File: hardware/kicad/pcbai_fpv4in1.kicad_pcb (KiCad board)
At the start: 6 copper layers, 85 x 70 mm, 253 parts, among them J1 BATT_PAD, J10 INA186A3IDCKR, J11 INA186A3IDCKR, J12 INA186A3IDCKR, J13 AT32F421K8T7, J14 DRV8300DRGER, J15 INA186A3IDCKR, J16 INA186A3IDCKR, J17 INA186A3IDCKR, J18 AT32F421K8T7, J19 DRV8300DRGER, J2 LMR51420YDDCR, J20 INA186A3IDCKR, J21 INA186A3IDCKR, J22 INA186A3IDCKR, J23 AT32F421K8T7, J24 DRV8300DRGER, J25 INA186A3IDCKR, J26 INA186A3IDCKR, J27 INA186A3IDCKR, J3 TLV76733DRVR, J4 SM08B-SRSS-TB, J5 USBLC6-2SC6, J6 USBLC6-2SC6, J7 USBLC6-2SC6, J8 AT32F421K8T7, J9 DRV8300DRGER, Q1 AON6260, Q10 AOTL66912, Q11 AOTL66912, Q12 AOTL66912, Q13 AOTL66912, Q14 AOTL66912, Q15 AOTL66912, Q16 AOTL66912, Q17 AOTL66912, Q18 AOTL66912, Q19 AOTL66912, Q2 AON6260, Q20 AOTL66912, Q21 AOTL66912, Q22 AOTL66912, Q23 AOTL66912, Q24 AOTL66912, Q25 AOTL66912, Q26 AOTL66912, Q27 AOTL66912, Q28 AOTL66912, Q3 AON6260, Q4 AON6260, Q5 AOTL66912, Q6 AOTL66912, Q7 AOTL66912, Q8 AOTL66912, Q9 AOTL66912

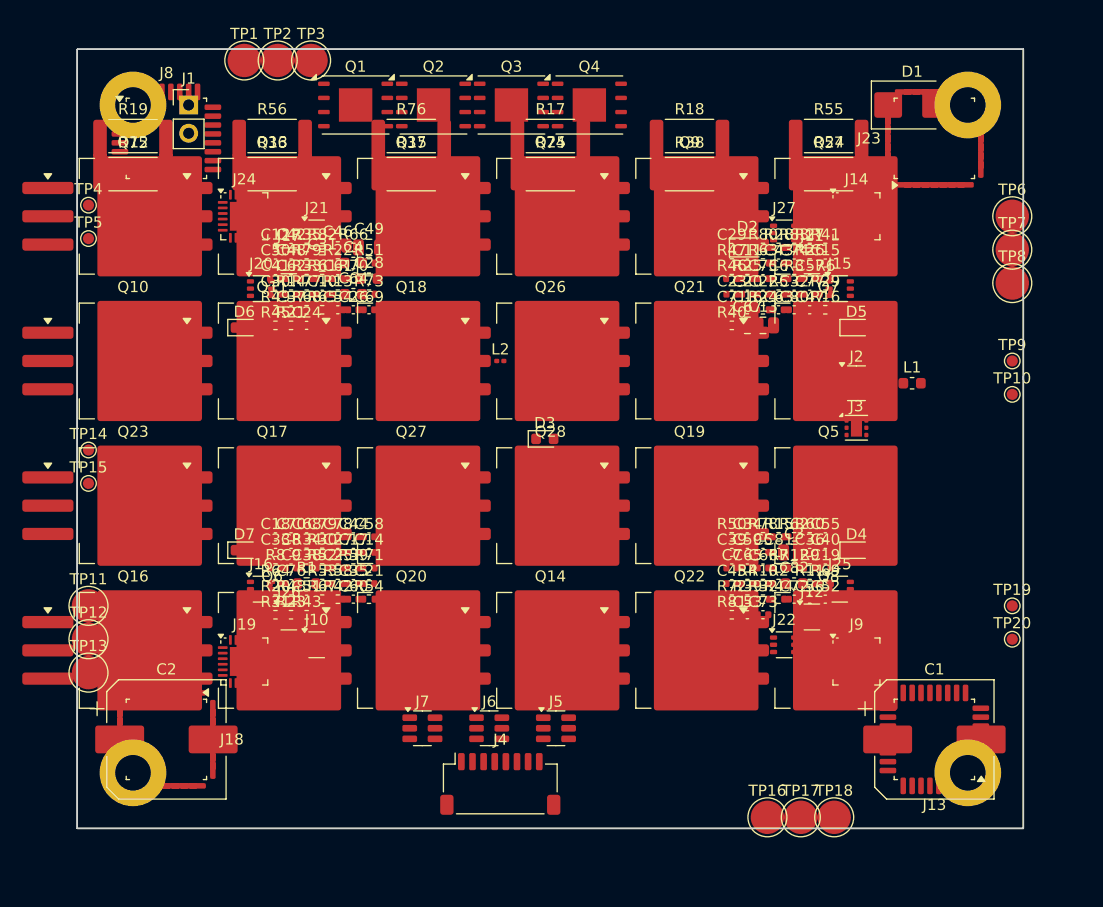
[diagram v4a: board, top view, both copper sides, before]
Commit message: Phase 4b-redo2: BEC placement integration (board 85×70 → 90×75)
Per master adjudication 2026-05-22: absorbed all Phase 2d-REDO BEC components
(5 bucks + LC + indicators + NTC + safety) + Phase 2e-REDO 16 solder pads
into the placement. Board grew 85×70 → 90×75 mm (+13.4% area for ~62% F.Cu
utilization, comfortable for routing).

Carry-forward from Phase 4b-REDO preserved:
  Per-MCU rotation: CH1=0°, CH2=90°, CH3=270°, CH4=180°
  FET-to-channel 3×2 corner sub-grids
  MOSFET (x,y) on B.Cu UNCHANGED → Phase 4c thermal verdict preserved
  Heatsink (80×55mm Al6061-T6) unchanged

New BEC placements:
  5 bucks (TPS54560 × 3 / AOZ1284 × 2) in middle band y=24..40, 5 columns
  Schottky catch diodes + eFuses/polyfuses + TVS + ferrites stacked per column
  NTC ICL (2× MF72 5D25 parallel) + indicator LEDs in battery section
  16 BEC solder pads on board edges (T7 verified, ≥2mm edge clearance)
  ~65 BEC supporting passives in lower-middle band y=44..56

Mount holes adjusted to new board: 4 at corners (5,5)/(85,5)/(5,70)/(85,70).
Custom 80×65 spacing pattern (commercial-product class per
feedback-anchor-on-most-capable-reference rule).

LED value naming disambiguated (Phase 4b parser conflict fixed):
  LED_PG: "GREEN" (V3V3 power-good, unchanged)
  LED_STATUS_x: "RED" (channel status, unchanged)
  LED_PWR: "GREEN_PWR" (NEW — battery present indicator)
  LED_RPOL: "RED_RPOL" (NEW — reverse-polarity warning)

place_board.py extended with categorization + placement for 10 new BEC
categories: ntc_icl, bec_buck_5v/9v, bec_schottky, bec_efuse, bec_polyfuse,
bec_tvs, bec_ferrite, bec_polymer_cap, bec_supervisor, bec_pad, led_pwr,
led_rpol.

Footprint corrections (kinet2pcb required standard KiCad library matches):
  Sunlord MWSA0630-2R2MT → MWSA0605S (close substitute)
  Sunlord MWSA0503S-1R5MT → MWSA0503S
  QFN-10-1EP_3x3mm_P0.5mm_EP1.65x1.65mm → DFN-10-1EP_3x3mm_P0.5mm_EP1.55x2.48mm
  R_Disc_D11.0mm_W4.6mm_P5.00mm → R_Axial_DIN0207_L6.3mm_D2.5mm_P5.08mm_Vertical

verify_placement.py 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
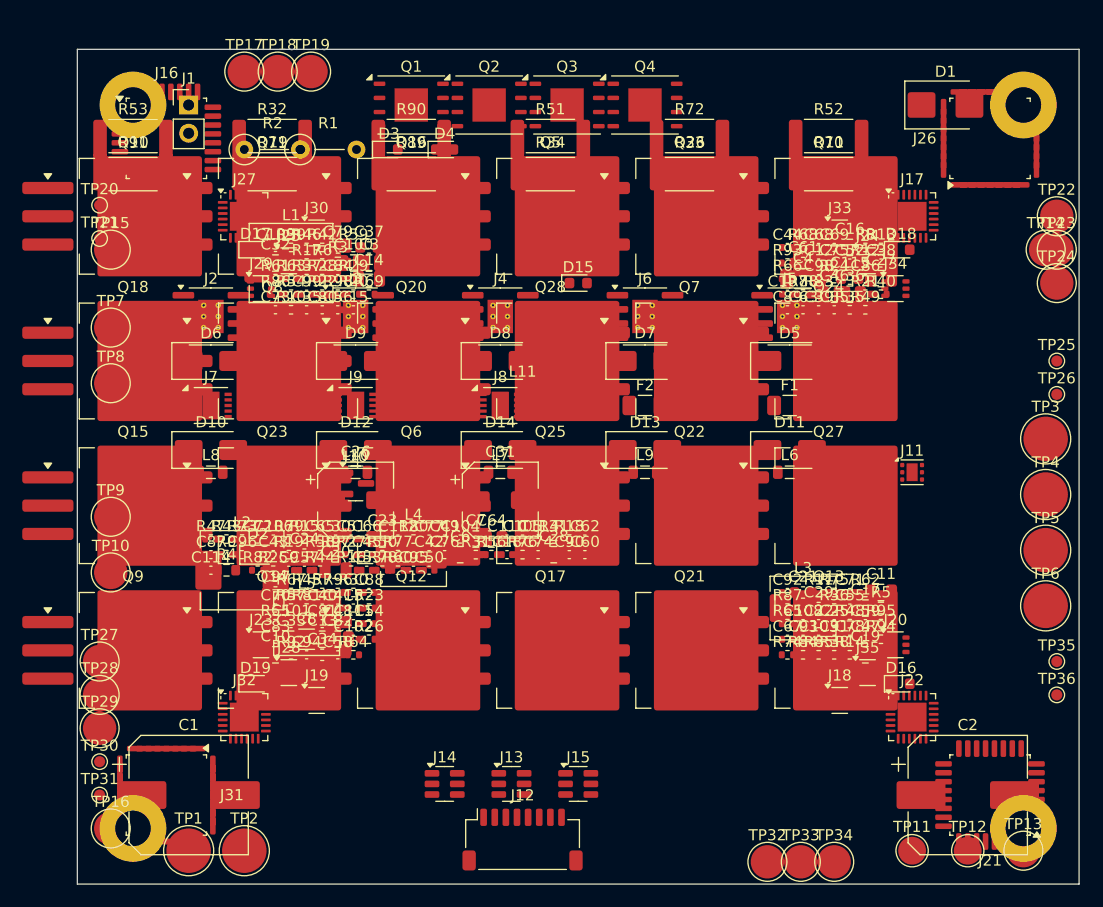
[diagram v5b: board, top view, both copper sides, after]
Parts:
- removed the ? at (80.0, 5.00)
- removed the ? at (5.00, 65.0)
- removed the ? at (80.0, 65.0)
- added ?: , MountingHole:MountingHole_3.2mm_M3, F.Cu at (85.0, 5.00)
- added ?: , MountingHole:MountingHole_3.2mm_M3, F.Cu at (5.00, 70.0)
- added ?: , MountingHole:MountingHole_3.2mm_M3, F.Cu at (85.0, 70.0)
- added C100: 10uF, Capacitor_SMD:C_0805_2012Metric, F.Cu at (24.8, 19.2)
- added C101: 100nF, Capacitor_SMD:C_0402_1005Metric, F.Cu at (19.2, 51.6)
- added C102: 1uF, Capacitor_SMD:C_0402_1005Metric, F.Cu at (24.8, 53.0)
- added C103: 100nF, Capacitor_SMD:C_0402_1005Metric, F.Cu at (66.6, 53.0)
- added C104: 1uF, Capacitor_SMD:C_0402_1005Metric, F.Cu at (34.4, 44.0)
- added C105: 100nF, Capacitor_SMD:C_0402_1005Metric, F.Cu at (40.0, 44.0)
- added C106: 1uF, Capacitor_SMD:C_0402_1005Metric, F.Cu at (17.6, 44.0)
- added C107: 1uF, Capacitor_SMD:C_0402_1005Metric, F.Cu at (63.8, 22.0)
- added C108: 1uF, Capacitor_SMD:C_0402_1005Metric, F.Cu at (65.2, 51.6)
- added C109: 100nF, Capacitor_SMD:C_0402_1005Metric, F.Cu at (17.8, 17.8)
- added C110: 100nF, Capacitor_SMD:C_0402_1005Metric, F.Cu at (38.6, 44.0)
- added C111: 100nF, Capacitor_SMD:C_0402_1005Metric, F.Cu at (24.8, 51.6)
- added C112: 1nF, Capacitor_SMD:C_0402_1005Metric, F.Cu at (28.8, 44.0)
- added C113: 1nF, Capacitor_SMD:C_0402_1005Metric, F.Cu at (41.4, 44.0)
- added C114: 1nF, Capacitor_SMD:C_0402_1005Metric, F.Cu at (12.0, 46.8)
- added C115: 22uF, Capacitor_SMD:C_0603_1608Metric, F.Cu at (69.4, 20.6)
- added C83: 100nF, Capacitor_SMD:C_0402_1005Metric, F.Cu at (17.8, 53.0)
- added C84: 1uF, Capacitor_SMD:C_0402_1005Metric, F.Cu at (23.4, 20.6)
- added C85: 100nF, Capacitor_SMD:C_0402_1005Metric, F.Cu at (68.0, 23.4)
- added C86: 1uF, Capacitor_SMD:C_0402_1005Metric, F.Cu at (70.8, 20.6)
- added C87: 100nF, Capacitor_SMD:C_0402_1005Metric, F.Cu at (12.0, 45.4)
- added C88: 1uF, Capacitor_SMD:C_0402_1005Metric, F.Cu at (26.2, 48.8)
- added C89: 1uF, Capacitor_SMD:C_0402_1005Metric, F.Cu at (63.8, 23.4)
- added C90: 1uF, Capacitor_SMD:C_0402_1005Metric, F.Cu at (44.2, 45.4)
- added C91: 100nF, Capacitor_SMD:C_0402_1005Metric, F.Cu at (68.0, 53.0)
- added C92: 100nF, Capacitor_SMD:C_0402_1005Metric, F.Cu at (63.8, 48.8)
- added C93: 100nF, Capacitor_SMD:C_0402_1005Metric, F.Cu at (65.2, 53.0)
- added C94: 1nF, Capacitor_SMD:C_0402_1005Metric, F.Cu at (20.6, 54.4)
- added C95: 1nF, Capacitor_SMD:C_0402_1005Metric, F.Cu at (30.2, 46.8)
- added C96: 1nF, Capacitor_SMD:C_0402_1005Metric, F.Cu at (14.8, 45.4)
- added C97: 22uF, Capacitor_SMD:C_0603_1608Metric, F.Cu at (17.8, 48.8)
- added C98: 100nF, Capacitor_SMD:C_0402_1005Metric, F.Cu at (66.6, 20.6)
- added C99: 100nF, Capacitor_SMD:C_0402_1005Metric, F.Cu at (20.6, 22.0)
- added D10: SMAJ5.0A, Diode_SMD:D_SMA, F.Cu at (12.0, 36.0)
- added D11: SMAJ5.0A, Diode_SMD:D_SMA, F.Cu at (64.0, 36.0)
- added D12: SMAJ5.0A, Diode_SMD:D_SMA, F.Cu at (25.0, 36.0)
- added D13: SMAJ9.0A, Diode_SMD:D_SMA, F.Cu at (51.0, 36.0)
- added D14: SMAJ9.0A, Diode_SMD:D_SMA, F.Cu at (38.0, 36.0)
- added D15: GREEN, LED_SMD:LED_0603_1608Metric, F.Cu at (45.0, 21.0)
- added D16: RED, LED_SMD:LED_0603_1608Metric, F.Cu at (74.0, 57.0)
- added D17: RED, LED_SMD:LED_0603_1608Metric, F.Cu at (16.0, 18.0)
- added D18: RED, LED_SMD:LED_0603_1608Metric, F.Cu at (74.0, 18.0)
- added D19: RED, LED_SMD:LED_0603_1608Metric, F.Cu at (16.0, 57.0)
- added D8: SS54, Diode_SMD:D_SMA, F.Cu at (38.0, 28.0)
- added D9: SS54, Diode_SMD:D_SMA, F.Cu at (25.0, 28.0)
- added F1: MF-MSMF200, Fuse:Fuse_1206_3216Metric, F.Cu at (64.0, 32.0)
- added F2: MF-MSMF200, Fuse:Fuse_1206_3216Metric, F.Cu at (51.0, 32.0)
- added J28: INA186A3IDCKR, Package_TO_SOT_SMD:SOT-363_SC-70-6, F.Cu at (19.0, 56.0)
- added J29: INA186A3IDCKR, Package_TO_SOT_SMD:SOT-363_SC-70-6, F.Cu at (16.5, 21.5)
- added J30: INA186A3IDCKR, Package_TO_SOT_SMD:SOT-363_SC-70-6, F.Cu at (21.5, 16.5)
- added J31: AT32F421K8T7, Package_QFP:LQFP-32_7x7mm_P0.8mm, F.Cu at (8.00, 67.0)
- added J32: DRV8300DRGER, Package_DFN_QFN:HVQFN-24-1EP_4x4mm_P0.5mm_EP2.6x2.6mm, F.Cu at (15.0, 60.0)
- added J33: INA186A3IDCKR, Package_TO_SOT_SMD:SOT-363_SC-70-6, F.Cu at (68.5, 16.5)
- added J34: INA186A3IDCKR, Package_TO_SOT_SMD:SOT-363_SC-70-6, F.Cu at (73.5, 21.5)
- added J35: INA186A3IDCKR, Package_TO_SOT_SMD:SOT-363_SC-70-6, F.Cu at (71.0, 56.0)
- added L10: 600ohm@100MHz, Inductor_SMD:L_0805_2012Metric, F.Cu at (25.0, 38.0)
- added L11: 120ohm@100MHz, Inductor_SMD:L_0201_0603Metric, F.Cu at (40.0, 30.0)
- added L3: 8.2uH, Inductor_SMD:L_Sunlord_MWSA0503S, F.Cu at (65.2, 50.2)
- added L4: 10uH, Inductor_SMD:L_Sunlord_MWSA0503S, F.Cu at (30.2, 45.4)
- added L5: 10uH, Inductor_SMD:L_Sunlord_MWSA0503S, F.Cu at (20.6, 51.6)
- added L6: 600ohm@100MHz, Inductor_SMD:L_0805_2012Metric, F.Cu at (64.0, 38.0)
- added L7: 600ohm@100MHz, Inductor_SMD:L_0805_2012Metric, F.Cu at (38.0, 38.0)
- added L8: 600ohm@100MHz, Inductor_SMD:L_0805_2012Metric, F.Cu at (12.0, 38.0)
- added L9: 600ohm@100MHz, Inductor_SMD:L_0805_2012Metric, F.Cu at (51.0, 38.0)
- added R84: 15R, Resistor_SMD:R_0402_1005Metric, F.Cu at (65.2, 54.4)
- added R85: 15R, Resistor_SMD:R_0402_1005Metric, F.Cu at (66.6, 54.4)
- added R86: 15R, Resistor_SMD:R_0402_1005Metric, F.Cu at (17.8, 22.0)
- added R87: 15R, Resistor_SMD:R_0402_1005Metric, F.Cu at (63.8, 50.2)
- added R88: 15R, Resistor_SMD:R_0402_1005Metric, F.Cu at (65.2, 22.0)
- added R89: 0.2mR, Resistor_SMD:R_2512_6332Metric, B.Cu at (30.0, 11.0)
- added R90: 0.2mR, Resistor_SMD:R_2512_6332Metric, B.Cu at (30.0, 8.00)
- added R91: 0.2mR, Resistor_SMD:R_2512_6332Metric, B.Cu at (5.00, 11.0)
- added R92: 22K, Resistor_SMD:R_0402_1005Metric, F.Cu at (19.2, 54.4)
- added R93: 3.3K, Resistor_SMD:R_0402_1005Metric, F.Cu at (63.8, 19.2)
- added R94: 22K, Resistor_SMD:R_0402_1005Metric, F.Cu at (72.2, 53.0)
- added R95: 3.3K, Resistor_SMD:R_0402_1005Metric, F.Cu at (72.2, 51.6)
- added R96: 22K, Resistor_SMD:R_0402_1005Metric, F.Cu at (23.4, 48.8)
- added R97: 3.3K, Resistor_SMD:R_0402_1005Metric, F.Cu at (23.2, 45.4)
- added R98: 1K, Resistor_SMD:R_0402_1005Metric, F.Cu at (23.4, 22.0)
- added TP21: SWCLK_CH1, TestPoint:TestPoint_Pad_D1.0mm, F.Cu at (2.00, 17.0)
- added TP22: MOTOR_A_CH2, TestPoint:TestPoint_Pad_D3.0mm, F.Cu at (88.0, 15.0)
- added TP23: MOTOR_B_CH2, TestPoint:TestPoint_Pad_D3.0mm, F.Cu at (88.0, 18.0)
- added TP24: MOTOR_C_CH2, TestPoint:TestPoint_Pad_D3.0mm, F.Cu at (88.0, 21.0)
- added TP25: SWDIO_CH2, TestPoint:TestPoint_Pad_D1.0mm, F.Cu at (88.0, 28.0)
- added TP26: SWCLK_CH2, TestPoint:TestPoint_Pad_D1.0mm, F.Cu at (88.0, 31.0)
- added TP27: MOTOR_A_CH3, TestPoint:TestPoint_Pad_D3.0mm, F.Cu at (2.00, 55.0)
- added TP28: MOTOR_B_CH3, TestPoint:TestPoint_Pad_D3.0mm, F.Cu at (2.00, 58.0)
- added TP29: MOTOR_C_CH3, TestPoint:TestPoint_Pad_D3.0mm, F.Cu at (2.00, 61.0)
- added TP30: SWDIO_CH3, TestPoint:TestPoint_Pad_D1.0mm, F.Cu at (2.00, 64.0)
- added TP31: SWCLK_CH3, TestPoint:TestPoint_Pad_D1.0mm, F.Cu at (2.00, 67.0)
- added TP32: MOTOR_A_CH4, TestPoint:TestPoint_Pad_D3.0mm, F.Cu at (62.0, 73.0)
- added TP33: MOTOR_B_CH4, TestPoint:TestPoint_Pad_D3.0mm, F.Cu at (65.0, 73.0)
- added TP34: MOTOR_C_CH4, TestPoint:TestPoint_Pad_D3.0mm, F.Cu at (68.0, 73.0)
- added TP35: SWDIO_CH4, TestPoint:TestPoint_Pad_D1.0mm, F.Cu at (88.0, 55.0)
- added TP36: SWCLK_CH4, TestPoint:TestPoint_Pad_D1.0mm, F.Cu at (88.0, 58.0)
- C10, C16, C23, C32, C36: value 100nF -> 22uF; footprint Capacitor_SMD:C_0402_1005Metric -> Capacitor_SMD:C_0805_2012Metric
- C11, C14: value 100nF -> 10uF; footprint Capacitor_SMD:C_0402_1005Metric -> Capacitor_SMD:C_0805_2012Metric
- C13: value 10uF -> 22uF
- C15, C35, C38, C51, C55, C56, C57, C69, C73, C74, C75: value 1uF -> 100nF
- C17, C7: value 1uF -> 10uF; footprint Capacitor_SMD:C_0402_1005Metric -> Capacitor_SMD:C_0805_2012Metric
- C19, C20, C33, C6: value 1uF -> 22uF; footprint Capacitor_SMD:C_0402_1005Metric -> Capacitor_SMD:C_0805_2012Metric
- C21, C37: value 1uF -> 10uF; footprint Capacitor_SMD:C_0402_1005Metric -> Capacitor_SMD:C_0603_1608Metric
- C24, C29, C34: value 100nF -> 10uF; footprint Capacitor_SMD:C_0402_1005Metric -> Capacitor_SMD:C_0603_1608Metric
- C25, C43, C44, C45, C62, C63, C80, C81: value 1nF -> 100nF
- C26: value 1nF -> 100uF_6V3_polymer; footprint Capacitor_SMD:C_0402_1005Metric -> Capacitor_SMD:CP_Elec_6.3x7.7
- C27: value 1nF -> 22uF; footprint Capacitor_SMD:C_0402_1005Metric -> Capacitor_SMD:C_0805_2012Metric
- C28: footprint Capacitor_SMD:C_0603_1608Metric -> Capacitor_SMD:C_0805_2012Metric
- C31: value 10uF -> 100uF_6V3_polymer; footprint Capacitor_SMD:C_0805_2012Metric -> Capacitor_SMD:CP_Elec_6.3x7.7
- C4: footprint Capacitor_SMD:C_0603_1608Metric -> Capacitor_SMD:C_1206_3216Metric
- C40, C41, C48, C50, C52, C54, C66, C68, C70, C72: value 100nF -> 1uF
- C46, C64, C82: value 22uF -> 10uF; footprint Capacitor_SMD:C_0603_1608Metric -> Capacitor_SMD:C_0805_2012Metric
- C49, C67: value 10uF -> 100nF; footprint Capacitor_SMD:C_0805_2012Metric -> Capacitor_SMD:C_0402_1005Metric
- C58, C59, C60, C76, C77, C78: value 100nF -> 1nF
- C61, C79: value 1nF -> 22uF; footprint Capacitor_SMD:C_0402_1005Metric -> Capacitor_SMD:C_0603_1608Metric
- C8: value 1uF -> 22uF; footprint Capacitor_SMD:C_0402_1005Metric -> Capacitor_SMD:C_1206_3216Metric
- D3: value GREEN -> GREEN_PWR
- D4: value RED -> RED_RPOL
- D5, D6, D7: value RED -> SS54; footprint LED_SMD:LED_0603_1608Metric -> Diode_SMD:D_SMA
- J10: value INA186A3IDCKR -> VSUP_5V_TBD; footprint Package_TO_SOT_SMD:SOT-363_SC-70-6 -> Package_TO_SOT_SMD:SOT-23
- J11: value INA186A3IDCKR -> TLV76733DRVR; footprint Package_TO_SOT_SMD:SOT-363_SC-70-6 -> Package_SON:WSON-6-1EP_2x2mm_P0.65mm_EP1x1.6mm
- J12: value INA186A3IDCKR -> SM08B-SRSS-TB; footprint Package_TO_SOT_SMD:SOT-363_SC-70-6 -> Connector_JST:JST_SH_SM08B-SRSS-TB_1x08-1MP_P1.00mm_Horizontal
- J13: value AT32F421K8T7 -> USBLC6-2SC6; footprint Package_QFP:LQFP-32_7x7mm_P0.8mm -> Package_TO_SOT_SMD:SOT-23-6
- J14: value DRV8300DRGER -> USBLC6-2SC6; footprint Package_DFN_QFN:HVQFN-24-1EP_4x4mm_P0.5mm_EP2.6x2.6mm -> Package_TO_SOT_SMD:SOT-23-6
- J15: value INA186A3IDCKR -> USBLC6-2SC6; footprint Package_TO_SOT_SMD:SOT-363_SC-70-6 -> Package_TO_SOT_SMD:SOT-23-6
- J16, J21, J26: value INA186A3IDCKR -> AT32F421K8T7; footprint Package_TO_SOT_SMD:SOT-363_SC-70-6 -> Package_QFP:LQFP-32_7x7mm_P0.8mm
- J17, J22, J27: value INA186A3IDCKR -> DRV8300DRGER; footprint Package_TO_SOT_SMD:SOT-363_SC-70-6 -> Package_DFN_QFN:HVQFN-24-1EP_4x4mm_P0.5mm_EP2.6x2.6mm
- J18, J23: value AT32F421K8T7 -> INA186A3IDCKR; footprint Package_QFP:LQFP-32_7x7mm_P0.8mm -> Package_TO_SOT_SMD:SOT-363_SC-70-6
- J19, J24: value DRV8300DRGER -> INA186A3IDCKR; footprint Package_DFN_QFN:HVQFN-24-1EP_4x4mm_P0.5mm_EP2.6x2.6mm -> Package_TO_SOT_SMD:SOT-363_SC-70-6
- J2: value LMR51420YDDCR -> TPS54560DDAR; footprint Package_TO_SOT_SMD:SOT-23-6 -> Package_SO:SOIC-8-1EP_3.9x4.9mm_P1.27mm_EP2.29x3mm_ThermalVias
- J3: value TLV76733DRVR -> TPS54560DDAR; footprint Package_SON:WSON-6-1EP_2x2mm_P0.65mm_EP1x1.6mm -> Package_SO:SOIC-8-1EP_3.9x4.9mm_P1.27mm_EP2.29x3mm_ThermalVias
- J4: value SM08B-SRSS-TB -> TPS54560DDAR; footprint Connector_JST:JST_SH_SM08B-SRSS-TB_1x08-1MP_P1.00mm_Horizontal -> Package_SO:SOIC-8-1EP_3.9x4.9mm_P1.27mm_EP2.29x3mm_ThermalVias
- J5, J6: value USBLC6-2SC6 -> AOZ1284PI; footprint Package_TO_SOT_SMD:SOT-23-6 -> Package_SO:SOIC-8-1EP_3.9x4.9mm_P1.27mm_EP2.29x3mm_ThermalVias
- J7: value USBLC6-2SC6 -> TPS259251DRCR; footprint Package_TO_SOT_SMD:SOT-23-6 -> Package_DFN_QFN:DFN-10-1EP_3x3mm_P0.5mm_EP1.55x2.48mm
- J8: value AT32F421K8T7 -> TPS259251DRCR; footprint Package_QFP:LQFP-32_7x7mm_P0.8mm -> Package_DFN_QFN:DFN-10-1EP_3x3mm_P0.5mm_EP1.55x2.48mm
- J9: value DRV8300DRGER -> TPS259251DRCR; footprint Package_DFN_QFN:HVQFN-24-1EP_4x4mm_P0.5mm_EP2.6x2.6mm -> Package_DFN_QFN:DFN-10-1EP_3x3mm_P0.5mm_EP1.55x2.48mm
- L1: value 0.47uH -> 4.7uH; footprint Inductor_SMD:L_0603_1608Metric -> Inductor_SMD:L_Sunlord_MWSA0605S
- L2: value 120ohm@100MHz -> 4.7uH; footprint Inductor_SMD:L_0201_0603Metric -> Inductor_SMD:L_Sunlord_MWSA0605S
- R1: value 10K -> MF72_5D25; footprint Resistor_SMD:R_0603_1608Metric -> Resistor_THT:R_Axial_DIN0207_L6.3mm_D2.5mm_P5.08mm_Vertical
- R10: value 40K -> 52K3
- R11, R13, R15, R16: value 15R -> 10K
- R12, R14: value 15R -> 102K
- R17, R18: value 0.2mR -> 10K; footprint Resistor_SMD:R_2512_6332Metric -> Resistor_SMD:R_0402_1005Metric; moved to F.Cu
- R19: value 0.2mR -> 1K; footprint Resistor_SMD:R_2512_6332Metric -> Resistor_SMD:R_0402_1005Metric; moved to F.Cu
- R2: value 130K -> MF72_5D25; footprint Resistor_SMD:R_0402_1005Metric -> Resistor_THT:R_Axial_DIN0207_L6.3mm_D2.5mm_P5.08mm_Vertical
- R20, R22: value 22K -> 100K
- R21: value 3.3K -> 14K
- R23, R42, R61, R80: value 3.3K -> 10K
- R24, R43, R62, R81: value 22K -> 10K
- R25, R44, R63, R82: value 3.3K -> 40K
- R26, R45, R64, R83: value 1K -> 15R
- R27, R28, R46, R47, R65, R66: value 10K -> 15R
- R29, R48, R67: value 40K -> 15R
- R3: value 24.9K -> 10K; footprint Resistor_SMD:R_0402_1005Metric -> Resistor_SMD:R_0603_1608Metric
- R32, R33, R34, R51, R52, R53, R70, R71, R72: value 15R -> 0.2mR; footprint Resistor_SMD:R_0402_1005Metric -> Resistor_SMD:R_2512_6332Metric; moved to B.Cu
- R35, R54, R73: value 15R -> 22K
- R36, R38, R55, R57, R74, R76: value 0.2mR -> 3.3K; footprint Resistor_SMD:R_2512_6332Metric -> Resistor_SMD:R_0402_1005Metric; moved to F.Cu
- R37, R56, R75: value 0.2mR -> 22K; footprint Resistor_SMD:R_2512_6332Metric -> Resistor_SMD:R_0402_1005Metric; moved to F.Cu
- R4: value 1K -> 5K1; footprint Resistor_SMD:R_0402_1005Metric -> Resistor_SMD:R_0603_1608Metric
- R41, R60, R79: value 22K -> 1K
- R5: value 100K -> 5K1; footprint Resistor_SMD:R_0402_1005Metric -> Resistor_SMD:R_0603_1608Metric
- R6: value 14K -> 52K3
- R7: value 100K -> 10K
- R8: value 10K -> 52K3
- TP1: value MOTOR_A_CH1 -> PAD_V5_FC_PLUS; footprint TestPoint:TestPoint_Pad_D3.0mm -> TestPoint:TestPoint_Pad_D4.0mm
- TP10: value SWCLK_CH2 -> PAD_V9_VTX2_GND; footprint TestPoint:TestPoint_Pad_D1.0mm -> TestPoint:TestPoint_Pad_D3.0mm
- TP11: value MOTOR_A_CH3 -> PAD_V3V3_PLUS; footprint TestPoint:TestPoint_Pad_D3.0mm -> TestPoint:TestPoint_Pad_D2.5mm
- TP12: value MOTOR_B_CH3 -> PAD_V3V3_GND; footprint TestPoint:TestPoint_Pad_D3.0mm -> TestPoint:TestPoint_Pad_D2.5mm
- TP13: value MOTOR_C_CH3 -> PAD_GND_DIST_1
- TP14: value SWDIO_CH3 -> PAD_GND_DIST_2; footprint TestPoint:TestPoint_Pad_D1.0mm -> TestPoint:TestPoint_Pad_D3.0mm
- TP15: value SWCLK_CH3 -> PAD_GND_DIST_3; footprint TestPoint:TestPoint_Pad_D1.0mm -> TestPoint:TestPoint_Pad_D3.0mm
- TP16: value MOTOR_A_CH4 -> PAD_GND_DIST_4
- TP17: value MOTOR_B_CH4 -> MOTOR_A_CH1
- TP18: value MOTOR_C_CH4 -> MOTOR_B_CH1
- TP19: value SWDIO_CH4 -> MOTOR_C_CH1; footprint TestPoint:TestPoint_Pad_D1.0mm -> TestPoint:TestPoint_Pad_D3.0mm
- TP2: value MOTOR_B_CH1 -> PAD_V5_FC_GND; footprint TestPoint:TestPoint_Pad_D3.0mm -> TestPoint:TestPoint_Pad_D4.0mm
- TP20: value SWCLK_CH4 -> SWDIO_CH1
- TP3: value MOTOR_C_CH1 -> PAD_V5_PI5_PLUS; footprint TestPoint:TestPoint_Pad_D3.0mm -> TestPoint:TestPoint_Pad_D4.0mm
- TP4: value SWDIO_CH1 -> PAD_V5_PI5_GND; footprint TestPoint:TestPoint_Pad_D1.0mm -> TestPoint:TestPoint_Pad_D4.0mm
- TP5: value SWCLK_CH1 -> PAD_V5_AI_PLUS; footprint TestPoint:TestPoint_Pad_D1.0mm -> TestPoint:TestPoint_Pad_D4.0mm
- TP6: value MOTOR_A_CH2 -> PAD_V5_AI_GND; footprint TestPoint:TestPoint_Pad_D3.0mm -> TestPoint:TestPoint_Pad_D4.0mm
- TP7: value MOTOR_B_CH2 -> PAD_V9_VTX1_PLUS
- TP8: value MOTOR_C_CH2 -> PAD_V9_VTX1_GND
- TP9: value SWDIO_CH2 -> PAD_V9_VTX2_PLUS; footprint TestPoint:TestPoint_Pad_D1.0mm -> TestPoint:TestPoint_Pad_D3.0mm
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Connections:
- C1 pad 1: +BATT -> +BATT_NTC
- C10 pad 1: VBAT_SENSE_OUT -> V_BUCK2_OUT
- C11 pad 1: +3V3 -> +BATT_NTC
- C12 pad 1: +3V3 -> BUCK3_BST
- C12 pad 2: GND -> BUCK3_SW
- C13 pad 1: +3V3 -> V_BUCK3_OUT
- C14 pad 1: +3V3A -> +BATT_NTC
- C15 pad 1: +3V3A -> BUCK4_BST
- C15 pad 2: GND -> BUCK4_SW
- C16 pad 1: NRST_CH1 -> V_BUCK4_OUT
- C17 pad 1: +5V -> +BATT_NTC
- C18 pad 1: +5V -> BUCK5_BST
- C18 pad 2: GND -> BUCK5_SW
- C19 pad 1: BSTA_CH1 -> V_BUCK5_OUT
- C19 pad 2: MOTOR_A_CH1 -> GND
- C2 pad 1: +BATT -> +BATT_NTC
- C20 pad 1: BSTB_CH1 -> +V5_FC
- C20 pad 2: MOTOR_B_CH1 -> GND
- C21 pad 1: BSTC_CH1 -> +V5_FC
- C21 pad 2: MOTOR_C_CH1 -> GND
- C22 pad 1: CSA_A_OUT_CH1 -> +V5_FC
- C23 pad 1: CSA_B_OUT_CH1 -> +V5_PI5
- C24 pad 1: CSA_C_OUT_CH1 -> +V5_PI5
- C25 pad 1: BEMF_A_CH1 -> +V5_PI5
- C26 pad 1: BEMF_B_CH1 -> +V5_PI5
- C27 pad 1: BEMF_C_CH1 -> +V5_PI5
- C28 pad 1: +5V -> +V5_AI
- C29 pad 1: +3V3 -> +V5_AI
- C3 pad 1: +BATT -> +BATT_NTC
- C30 pad 1: +3V3 -> +V5_AI
- C31 pad 1: +3V3 -> +V5_AI
- C32 pad 1: +3V3A -> +V5_AI
- C33 pad 1: +3V3A -> +V9_VTX1
- C34 pad 1: NRST_CH2 -> +V9_VTX1
- C35 pad 1: +5V -> +V9_VTX1
- C36 pad 1: +5V -> +V9_VTX2
- C37 pad 1: BSTA_CH2 -> +V9_VTX2
- C37 pad 2: MOTOR_A_CH2 -> GND
- C38 pad 1: BSTB_CH2 -> +V9_VTX2
- C38 pad 2: MOTOR_B_CH2 -> GND
- C39 pad 1: BSTC_CH2 -> +V5_FC
- C39 pad 2: MOTOR_C_CH2 -> GND
- C4 pad 1: +5V -> +BATT_NTC
- C40 pad 1: CSA_A_OUT_CH2 -> +3V3
- C41 pad 1: CSA_B_OUT_CH2 -> +3V3A
- C42 pad 1: CSA_C_OUT_CH2 -> +3V3A
- C43 pad 1: BEMF_A_CH2 -> VBAT_SENSE_OUT
- C44 pad 1: BEMF_B_CH2 -> +3V3
- C45 pad 1: BEMF_C_CH2 -> +3V3
- C46 pad 1: +5V -> +3V3
- C47 pad 1: +3V3 -> +3V3A
- C48 pad 1: +3V3 -> +3V3A
- C49 pad 1: +3V3 -> NRST_CH1
- C5 pad 1: BUCK_BST -> BUCK1_BST
- C5 pad 2: BUCK_SW -> BUCK1_SW
- C50 pad 1: +3V3A -> +V5_FC
- C51 pad 1: +3V3A -> +V5_FC
- C52 pad 1: NRST_CH3 -> BSTA_CH1
- C52 pad 2: GND -> MOTOR_A_CH1
- C53 pad 1: +5V -> BSTB_CH1
- C53 pad 2: GND -> MOTOR_B_CH1
- C54 pad 1: +5V -> BSTC_CH1
- C54 pad 2: GND -> MOTOR_C_CH1
- C55 pad 1: BSTA_CH3 -> CSA_A_OUT_CH1
- C55 pad 2: MOTOR_A_CH3 -> GND
- C56 pad 1: BSTB_CH3 -> CSA_B_OUT_CH1
- C56 pad 2: MOTOR_B_CH3 -> GND
- C57 pad 1: BSTC_CH3 -> CSA_C_OUT_CH1
- C57 pad 2: MOTOR_C_CH3 -> GND
- C58 pad 1: CSA_A_OUT_CH3 -> BEMF_A_CH1
- C59 pad 1: CSA_B_OUT_CH3 -> BEMF_B_CH1
- C6 pad 1: +5V -> V_BUCK1_OUT
- C60 pad 1: CSA_C_OUT_CH3 -> BEMF_C_CH1
- C61 pad 1: BEMF_A_CH3 -> +V5_FC
- C62 pad 1: BEMF_B_CH3 -> +3V3
- C63 pad 1: BEMF_C_CH3 -> +3V3
- C64 pad 1: +5V -> +3V3
- C65 pad 1: +3V3 -> +3V3A
- C66 pad 1: +3V3 -> +3V3A
- C67 pad 1: +3V3 -> NRST_CH2
- C68 pad 1: +3V3A -> +V5_FC
- C69 pad 1: +3V3A -> +V5_FC
- C7 pad 1: +3V3 -> +BATT_NTC
- C70 pad 1: NRST_CH4 -> BSTA_CH2
- C70 pad 2: GND -> MOTOR_A_CH2
- C71 pad 1: +5V -> BSTB_CH2
- C71 pad 2: GND -> MOTOR_B_CH2
- C72 pad 1: +5V -> BSTC_CH2
- C72 pad 2: GND -> MOTOR_C_CH2
- C73 pad 1: BSTA_CH4 -> CSA_A_OUT_CH2
- C73 pad 2: MOTOR_A_CH4 -> GND
- C74 pad 1: BSTB_CH4 -> CSA_B_OUT_CH2
- C74 pad 2: MOTOR_B_CH4 -> GND
- C75 pad 1: BSTC_CH4 -> CSA_C_OUT_CH2
- C75 pad 2: MOTOR_C_CH4 -> GND
- C76 pad 1: CSA_A_OUT_CH4 -> BEMF_A_CH2
- C77 pad 1: CSA_B_OUT_CH4 -> BEMF_B_CH2
- C78 pad 1: CSA_C_OUT_CH4 -> BEMF_C_CH2
- C79 pad 1: BEMF_A_CH4 -> +V5_FC
- C8 pad 1: +3V3A -> +BATT_NTC
- C80 pad 1: BEMF_B_CH4 -> +3V3
- C81 pad 1: BEMF_C_CH4 -> +3V3
- C82 pad 1: +5V -> +3V3
- C9 pad 1: +3V3A -> BUCK2_BST
- C9 pad 2: GND -> BUCK2_SW
- D1 pad 2: +BATT -> +BATT_NTC
- D3 pad 2: LED_PG_NODE -> LED_PWR_NODE
- D4 pad 1: LED_GPIO_CH1 -> BATGND
- D4 pad 2: N$8 -> LED_RPOL_NODE
- D5 pad 1: LED_GPIO_CH2 -> GND
- D5 pad 2: N$16 -> BUCK1_SW
- D6 pad 1: LED_GPIO_CH3 -> GND
- D6 pad 2: N$24 -> BUCK2_SW
- D7 pad 1: LED_GPIO_CH4 -> GND
- D7 pad 2: N$32 -> BUCK3_SW
- J10 pad 1: SHUNT_A_TOP_CH1 -> +V5_PI5
- J10 pad 3: GND -> PG_RPI
- J11 pad 1: SHUNT_B_TOP_CH1 -> +V5_FC
- J11 pad 3: GND -> +V5_FC
- J11 pad 4: +3V3 -> (no net)
- J11 pad 5: CSA_B_OUT_CH1 -> +3V3
- J11 pad 6: GND -> (no net)
- J12 pad 1: SHUNT_C_TOP_CH1 -> GND
- J12 pad 2: GND -> VBAT_SENSE_OUT
- J12 pad 3: GND -> CURR_OUT
- J12 pad 4: +3V3 -> TLM
- J12 pad 5: CSA_C_OUT_CH1 -> M4_RAW
- J12 pad 6: GND -> M3_CLEAN
- J13 pad 1: +3V3 -> M1_CLEAN
- J13 pad 2: PF0_NC_CH2 -> GND
- J13 pad 3: PF1_NC_CH2 -> +V5_FC
- J13 pad 4: NRST_CH2 -> M2_RAW
- J13 pad 5: +3V3A -> GND
- J13 pad 6: BEMF_A_CH2 -> M1_CLEAN
- J14 pad 1: PWM_INLA_CH2 -> M3_CLEAN
- J14 pad 2: PWM_INLB_CH2 -> GND
- J14 pad 3: PWM_INLC_CH2 -> +V5_FC
- J14 pad 4: +5V -> M4_RAW
- J14 pad 6: GND -> M3_CLEAN
- J15 pad 1: SHUNT_A_TOP_CH2 -> TLM
- J15 pad 3: GND -> +V5_FC
- J15 pad 4: +3V3 -> ESD_SPARE
- J15 pad 5: CSA_A_OUT_CH2 -> GND
- J15 pad 6: GND -> TLM
- J16 pad 1: SHUNT_B_TOP_CH2 -> +3V3
- J16 pad 2: GND -> PF0_NC_CH1
- J16 pad 3: GND -> PF1_NC_CH1
- J16 pad 4: +3V3 -> NRST_CH1
- J16 pad 5: CSA_B_OUT_CH2 -> +3V3A
- J16 pad 6: GND -> BEMF_A_CH1
- J17 pad 1: SHUNT_C_TOP_CH2 -> PWM_INLA_CH1
- J17 pad 2: GND -> PWM_INLB_CH1
- J17 pad 3: GND -> PWM_INLC_CH1
- J17 pad 4: +3V3 -> +V5_FC
- J17 pad 5: CSA_C_OUT_CH2 -> GND
- J18 pad 1: +3V3 -> SHUNT_A_TOP_CH1
- J18 pad 2: PF0_NC_CH3 -> GND
- J18 pad 3: PF1_NC_CH3 -> GND
- J18 pad 4: NRST_CH3 -> +3V3
- J18 pad 5: +3V3A -> CSA_A_OUT_CH1
- J18 pad 6: BEMF_A_CH3 -> GND
- J19 pad 1: PWM_INLA_CH3 -> SHUNT_B_TOP_CH1
- J19 pad 2: PWM_INLB_CH3 -> GND
- J19 pad 3: PWM_INLC_CH3 -> GND
- J19 pad 4: +5V -> +3V3
- J19 pad 5: GND -> CSA_B_OUT_CH1
- J2 pad 1: BUCK_SW -> BUCK1_BST
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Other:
- board size 85 x 70 mm -> 90 x 75 mm

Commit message: Phase 3b-detail: silkscreen + BOOT0 + TLM pull-up + strain-relief + fiducials
Closes 6 small gaps from earlier phases per Sai 2026-05-22 authorization.

1. Telemetry pull-up: 4× 10kΩ on PB6 to +3V3.
   Rigor §5b finding (AM32/Mcu/f421/Src/serial_telemetry.c L27-34):
   PB6 is PUSH-PULL + internal pull-up + half-duplex single-line — NOT
   open-drain as master preamble claimed. URGENT raised + worker added
   external pull-up anyway per FPV-reference noise-immunity standard. If
   master picks option (b) [skip pull-up], revert is single SKiDL line.

2. BOOT0 emergency-DFU access: 4× 10kΩ pull-down + 4× 2-pin jumper pads
   (BOOT_JUMPER + BOOT_3V) per channel. Default = boot from flash;
   solder-bridge jumper to enter system bootloader for recovery flash.

3. Motor pad strain-relief: 12 outer copper rings (D 5mm, F.Cu) + 48 spokes
   (4 per pad at 45° offsets). Inner D 3mm pad preserved. Increases solder
   area + provides thermal-spoke heat-sinking pattern.

4. PL1 conformal coating: REQUIREMENTS §reliability-spec PL1 subsection.
   MG Chemicals 4223 or equivalent; optional indoor, recommended outdoor/wet.

5. Silkscreen labels: 124 gr_text on F.SilkS / B.SilkS via
   apply_silkscreen.py script. Channel IDs, motor labels (A/B/C × 4),
   battery (BAT+), NTC ICL, BEC pad polarity + rail tag (16 pads), indicator
   LEDs (PWR/REV!), FC connector pinout (header + 8 per-pin labels), SWD
   per-channel, mount holes (M3), PCB rev (Rev A), project mark
   (pcb.ai FPV4in1 v0), manufacturer placeholder ([MFR-MARK]), 24
   per-MOSFET thermal-pad orientation markers (TP+arrow) on B.SilkS, +
   single 'THERMAL PADS UP TO HEATSINK' zone label.

6. Manufacturing fiducials: 3× F.Cu + 3× B.Cu fiducial copper dots
   (D 1mm copper + D 2mm mask opening) at clear board positions.

Note on FC silkscreen string: master contract said 'D1 D2 D3 D4 TLM BAT+ GND
+5V' but SKiDL J_FC pin order is GND/VBAT/CURR/TLM/M4/M3/M2/M1 (pins 1-8).
Worker used SKiDL actual pin order; URGENT raised for con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
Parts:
- added R100: 22K, Resistor_SMD:R_0402_1005Metric, F.Cu at (24.8, 19.2)
- added R101: 3.3K, Resistor_SMD:R_0402_1005Metric, F.Cu at (42.8, 45.4)
- added R102: 22K, Resistor_SMD:R_0402_1005Metric, F.Cu at (16.2, 45.4)
- added R103: 3.3K, Resistor_SMD:R_0402_1005Metric, F.Cu at (69.4, 20.6)
- added R104: 22K, Resistor_SMD:R_0402_1005Metric, F.Cu at (20.6, 17.8)
- added R105: 3.3K, Resistor_SMD:R_0402_1005Metric, F.Cu at (65.2, 22.0)
- added R106: 1K, Resistor_SMD:R_0402_1005Metric, F.Cu at (70.8, 22.0)
- added R99: 0.2mR, Resistor_SMD:R_2512_6332Metric, B.Cu at (30.0, 8.00)
- added TP37: SWCLK_CH3, TestPoint:TestPoint_Pad_D1.0mm, F.Cu at (2.00, 67.0)
- added TP38: BOOT_JUMPER_CH4, TestPoint:TestPoint_Pad_D1.5mm, F.Cu at (20.6, 50.2)
- added TP39: BOOT_3V_CH4, TestPoint:TestPoint_Pad_D1.5mm, F.Cu at (20.4, 45.4)
- added TP40: MOTOR_A_CH4, TestPoint:TestPoint_Pad_D3.0mm, F.Cu at (62.0, 73.0)
- added TP41: MOTOR_B_CH4, TestPoint:TestPoint_Pad_D3.0mm, F.Cu at (65.0, 73.0)
- added TP42: MOTOR_C_CH4, TestPoint:TestPoint_Pad_D3.0mm, F.Cu at (68.0, 73.0)
- added TP43: SWDIO_CH4, TestPoint:TestPoint_Pad_D1.0mm, F.Cu at (88.0, 55.0)
- added TP44: SWCLK_CH4, TestPoint:TestPoint_Pad_D1.0mm, F.Cu at (88.0, 58.0)
- R25, R44: value 40K -> 10K
- R26, R45, R46, R47, R65, R66, R67, R68, R86, R87, R88: value 15R -> 10K
- R27, R48, R69: value 15R -> 40K
- R32, R33, R51, R52, R53, R70, R71, R72, R91: value 0.2mR -> 15R; footprint Resistor_SMD:R_2512_6332Metric -> Resistor_SMD:R_0402_1005Metric; moved to F.Cu
- R35, R56, R77: value 22K -> 0.2mR; footprint Resistor_SMD:R_0402_1005Metric -> Resistor_SMD:R_2512_6332Metric; moved to B.Cu
- R36, R55, R57, R76, R78, R97: value 3.3K -> 0.2mR; footprint Resistor_SMD:R_0402_1005Metric -> Resistor_SMD:R_2512_6332Metric; moved to B.Cu
- R41, R60, R79: value 1K -> 22K
- R42, R61, R80: value 10K -> 3.3K
- R43: value 10K -> 1K
- R54, R73, R75, R92, R94, R96: value 22K -> 15R
- R62, R81: value 10K -> 22K
- R63, R82: value 40K -> 3.3K
- R64, R85: value 15R -> 1K
- R74, R93, R95: value 3.3K -> 15R
- R83: value 15R -> 22K
- R84: value 15R -> 3.3K
- R89: value 0.2mR -> 10K; footprint Resistor_SMD:R_2512_6332Metric -> Resistor_SMD:R_0402_1005Metric; moved to F.Cu
- R90: value 0.2mR -> 40K; footprint Resistor_SMD:R_2512_6332Metric -> Resistor_SMD:R_0402_1005Metric; moved to F.Cu
- R98: value 1K -> 0.2mR; footprint Resistor_SMD:R_0402_1005Metric -> Resistor_SMD:R_2512_6332Metric; moved to B.Cu
- TP17: value MOTOR_A_CH1 -> BOOT_JUMPER_CH1; footprint TestPoint:TestPoint_Pad_D3.0mm -> TestPoint:TestPoint_Pad_D1.5mm
- TP18: value MOTOR_B_CH1 -> BOOT_3V_CH1; footprint TestPoint:TestPoint_Pad_D3.0mm -> TestPoint:TestPoint_Pad_D1.5mm
- TP19: value MOTOR_C_CH1 -> MOTOR_A_CH1
- TP20: value SWDIO_CH1 -> MOTOR_B_CH1; footprint TestPoint:TestPoint_Pad_D1.0mm -> TestPoint:TestPoint_Pad_D3.0mm
- TP21: value SWCLK_CH1 -> MOTOR_C_CH1; footprint TestPoint:TestPoint_Pad_D1.0mm -> TestPoint:TestPoint_Pad_D3.0mm
- TP22: value MOTOR_A_CH2 -> SWDIO_CH1; footprint TestPoint:TestPoint_Pad_D3.0mm -> TestPoint:TestPoint_Pad_D1.0mm
- TP23: value MOTOR_B_CH2 -> SWCLK_CH1; footprint TestPoint:TestPoint_Pad_D3.0mm -> TestPoint:TestPoint_Pad_D1.0mm
- TP24: value MOTOR_C_CH2 -> BOOT_JUMPER_CH2; footprint TestPoint:TestPoint_Pad_D3.0mm -> TestPoint:TestPoint_Pad_D1.5mm
- TP25: value SWDIO_CH2 -> BOOT_3V_CH2; footprint TestPoint:TestPoint_Pad_D1.0mm -> TestPoint:TestPoint_Pad_D1.5mm
- TP26: value SWCLK_CH2 -> MOTOR_A_CH2; footprint TestPoint:TestPoint_Pad_D1.0mm -> TestPoint:TestPoint_Pad_D3.0mm
- TP27: value MOTOR_A_CH3 -> MOTOR_B_CH2
- TP28: value MOTOR_B_CH3 -> MOTOR_C_CH2
- TP29: value MOTOR_C_CH3 -> SWDIO_CH2; footprint TestPoint:TestPoint_Pad_D3.0mm -> TestPoint:TestPoint_Pad_D1.0mm
- TP30: value SWDIO_CH3 -> SWCLK_CH2
- TP31: value SWCLK_CH3 -> BOOT_JUMPER_CH3; footprint TestPoint:TestPoint_Pad_D1.0mm -> TestPoint:TestPoint_Pad_D1.5mm
- TP32: value MOTOR_A_CH4 -> BOOT_3V_CH3; footprint TestPoint:TestPoint_Pad_D3.0mm -> TestPoint:TestPoint_Pad_D1.5mm
- TP33: value MOTOR_B_CH4 -> MOTOR_A_CH3
- TP34: value MOTOR_C_CH4 -> MOTOR_B_CH3
- TP35: value SWDIO_CH4 -> MOTOR_C_CH3; footprint TestPoint:TestPoint_Pad_D1.0mm -> TestPoint:TestPoint_Pad_D3.0mm
- TP36: value SWCLK_CH4 -> SWDIO_CH3
- moved TP27 93.6 mm to (88.0, 18.0)
- moved TP28 93.6 mm to (88.0, 21.0)
- moved TP29 92.1 mm to (88.0, 28.0)
- moved TP30 92.1 mm to (88.0, 31.0)
- moved TP35 86.2 mm to (2.00, 61.0)
- moved TP36 86.2 mm to (2.00, 64.0)
- moved TP22 86.0 mm to (2.00, 14.0)
- moved TP23 86.0 mm to (2.00, 17.0)
- moved R53 77.0 mm to (69.4, 50.2)
- moved J27 75.0 mm to (75.0, 60.0)
- moved R36 74.2 mm to (5.00, 11.0)
- moved J16 74.0 mm to (82.0, 8.00), turned to 90 degrees
- moved J21 74.0 mm to (8.00, 67.0), turned to 270 degrees
- moved TP17 73.7 mm to (70.8, 50.2)
- moved TP18 73.5 mm to (72.2, 51.6)
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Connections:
- J16 pad 31: GND -> BOOT0_CH1
- J21 pad 31: GND -> BOOT0_CH2
- J26 pad 31: GND -> BOOT0_CH3
- J31 pad 31: GND -> BOOT0_CH4
- R23 pad 1: NRST_CH1 -> BOOT0_CH1
- R23 pad 2: +3V3 -> GND
- R24 pad 1: GND -> TLM
- R24 pad 2: GND -> +3V3
- R25 pad 1: N$4 -> NRST_CH1
- R25 pad 2: GND -> +3V3
- R26 pad 1: GHA_CH1 -> BOOT0_CH1
- R26 pad 2: N$5 (its old number) -> GND
- R27 pad 1: GLA_CH1 -> N$4
- R27 pad 2: N$6 (its old number) -> GND
- R28 pad 1: GHB_CH1 -> GHA_CH1
- R29 pad 1: GLB_CH1 -> GLA_CH1
- R30 pad 1: GHC_CH1 -> GHB_CH1
- R31 pad 1: GLC_CH1 -> GLB_CH1
- R32 pad 1: SHUNT_A_TOP_CH1 -> GHC_CH1
- R32 pad 2: GND -> N$9
- R33 pad 1: SHUNT_B_TOP_CH1 -> GLC_CH1
- R33 pad 2: GND -> N$10
- R34 pad 1: SHUNT_C_TOP_CH1 -> SHUNT_A_TOP_CH1
- R35 pad 1: MOTOR_A_CH1 -> SHUNT_B_TOP_CH1
- R35 pad 2: BEMF_A_CH1 -> GND
- R36 pad 1: BEMF_A_CH1 -> SHUNT_C_TOP_CH1
- R37 pad 1: MOTOR_B_CH1 -> MOTOR_A_CH1
- R37 pad 2: BEMF_B_CH1 -> BEMF_A_CH1
- R38 pad 1: BEMF_B_CH1 -> BEMF_A_CH1
- R39 pad 1: MOTOR_C_CH1 -> MOTOR_B_CH1
- R39 pad 2: BEMF_C_CH1 -> BEMF_B_CH1
- R40 pad 1: BEMF_C_CH1 -> BEMF_B_CH1
- R41 pad 1: +3V3 -> MOTOR_C_CH1
- R41 pad 2: N$11 -> BEMF_C_CH1
- R42 pad 1: NRST_CH2 -> BEMF_C_CH1
- R42 pad 2: +3V3 -> GND
- R43 pad 1: GND -> +3V3
- R43 pad 2: GND -> N$11
- R44 pad 1: N$12 -> BOOT0_CH2
- R45 pad 1: GHA_CH2 -> TLM
- R45 pad 2: N$13 (its old number) -> +3V3
- R46 pad 1: GLA_CH2 -> NRST_CH2
- R46 pad 2: N$14 (its old number) -> +3V3
- R47 pad 1: GHB_CH2 -> BOOT0_CH2
- R47 pad 2: N$15 -> GND
- R48 pad 1: GLB_CH2 -> N$12
- R48 pad 2: N$16 -> GND
- R49 pad 1: GHC_CH2 -> GHA_CH2
- R50 pad 1: GLC_CH2 -> GLA_CH2
- R51 pad 1: SHUNT_A_TOP_CH2 -> GHB_CH2
- R51 pad 2: GND -> N$15
- R52 pad 1: SHUNT_B_TOP_CH2 -> GLB_CH2
- R52 pad 2: GND -> N$16
- R53 pad 1: SHUNT_C_TOP_CH2 -> GHC_CH2
- R53 pad 2: GND -> N$17
- R54 pad 1: MOTOR_A_CH2 -> GLC_CH2
- R54 pad 2: BEMF_A_CH2 -> N$18
- R55 pad 1: BEMF_A_CH2 -> SHUNT_A_TOP_CH2
- R56 pad 1: MOTOR_B_CH2 -> SHUNT_B_TOP_CH2
- R56 pad 2: BEMF_B_CH2 -> GND
- R57 pad 1: BEMF_B_CH2 -> SHUNT_C_TOP_CH2
- R58 pad 1: MOTOR_C_CH2 -> MOTOR_A_CH2
- R58 pad 2: BEMF_C_CH2 -> BEMF_A_CH2
- R59 pad 1: BEMF_C_CH2 -> BEMF_A_CH2
- R60 pad 1: +3V3 -> MOTOR_B_CH2
- R60 pad 2: N$19 -> BEMF_B_CH2
- R61 pad 1: NRST_CH3 -> BEMF_B_CH2
- R61 pad 2: +3V3 -> GND
- R62 pad 1: GND -> MOTOR_C_CH2
- R62 pad 2: GND -> BEMF_C_CH2
- R63 pad 1: N$20 -> BEMF_C_CH2
- R64 pad 1: GHA_CH3 -> +3V3
- R64 pad 2: N$21 -> N$19
- R65 pad 1: GLA_CH3 -> BOOT0_CH3
- R65 pad 2: N$22 -> GND
- R66 pad 1: GHB_CH3 -> TLM
- R66 pad 2: N$23 -> +3V3
- R67 pad 1: GLB_CH3 -> NRST_CH3
- R67 pad 2: N$24 -> +3V3
- R68 pad 1: GHC_CH3 -> BOOT0_CH3
- R68 pad 2: N$25 -> GND
- R69 pad 1: GLC_CH3 -> N$20
- R69 pad 2: N$26 -> GND
- R70 pad 1: SHUNT_A_TOP_CH3 -> GHA_CH3
- R70 pad 2: GND -> N$21
- R71 pad 1: SHUNT_B_TOP_CH3 -> GLA_CH3
- R71 pad 2: GND -> N$22
- R72 pad 1: SHUNT_C_TOP_CH3 -> GHB_CH3
- R72 pad 2: GND -> N$23
- R73 pad 1: MOTOR_A_CH3 -> GLB_CH3
- R73 pad 2: BEMF_A_CH3 -> N$24
- R74 pad 1: BEMF_A_CH3 -> GHC_CH3
- R74 pad 2: GND -> N$25
- R75 pad 1: MOTOR_B_CH3 -> GLC_CH3
- R75 pad 2: BEMF_B_CH3 -> N$26
- R76 pad 1: BEMF_B_CH3 -> SHUNT_A_TOP_CH3
- R77 pad 1: MOTOR_C_CH3 -> SHUNT_B_TOP_CH3
- R77 pad 2: BEMF_C_CH3 -> GND
- R78 pad 1: BEMF_C_CH3 -> SHUNT_C_TOP_CH3
- R79 pad 1: +3V3 -> MOTOR_A_CH3
- R79 pad 2: N$27 -> BEMF_A_CH3
- R80 pad 1: NRST_CH4 -> BEMF_A_CH3
- R80 pad 2: +3V3 -> GND
- R81 pad 1: GND -> MOTOR_B_CH3
- R81 pad 2: GND -> BEMF_B_CH3
- R82 pad 1: N$28 -> BEMF_B_CH3
- R83 pad 1: GHA_CH4 -> MOTOR_C_CH3
- R83 pad 2: N$29 -> BEMF_C_CH3
- R84 pad 1: GLA_CH4 -> BEMF_C_CH3
- R84 pad 2: N$30 -> GND
- R85 pad 1: GHB_CH4 -> +3V3
- R85 pad 2: N$31 -> N$27
- R86 pad 1: GLB_CH4 -> BOOT0_CH4
- R86 pad 2: N$32 -> GND
- R87 pad 1: GHC_CH4 -> TLM
- R87 pad 2: N$33 -> +3V3
- R88 pad 1: GLC_CH4 -> NRST_CH4
- R88 pad 2: N$34 -> +3V3
- R89 pad 1: SHUNT_A_TOP_CH4 -> BOOT0_CH4
- R90 pad 1: SHUNT_B_TOP_CH4 -> N$28
- R91 pad 1: SHUNT_C_TOP_CH4 -> GHA_CH4
- R91 pad 2: GND -> N$29
- R92 pad 1: MOTOR_A_CH4 -> GLA_CH4
- R92 pad 2: BEMF_A_CH4 -> N$30
- R93 pad 1: BEMF_A_CH4 -> GHB_CH4
- R93 pad 2: GND -> N$31
- R94 pad 1: MOTOR_B_CH4 -> GLB_CH4
- R94 pad 2: BEMF_B_CH4 -> N$32
- R95 pad 1: BEMF_B_CH4 -> GHC_CH4
- R95 pad 2: GND -> N$33
- R96 pad 1: MOTOR_C_CH4 -> GLC_CH4
- R96 pad 2: BEMF_C_CH4 -> N$34
- R97 pad 1: BEMF_C_CH4 -> SHUNT_A_TOP_CH4
- R98 pad 1: +3V3 -> SHUNT_B_TOP_CH4
- R98 pad 2: N$35 -> GND
- TP17 pad 1: MOTOR_A_CH1 -> BOOT0_CH1
- TP18 pad 1: MOTOR_B_CH1 -> +3V3
- TP19 pad 1: MOTOR_C_CH1 -> MOTOR_A_CH1
- TP20 pad 1: SWDIO_CH1 -> MOTOR_B_CH1
- TP21 pad 1: SWCLK_CH1 -> MOTOR_C_CH1
- TP22 pad 1: MOTOR_A_CH2 -> SWDIO_CH1
- TP23 pad 1: MOTOR_B_CH2 -> SWCLK_CH1
- TP24 pad 1: MOTOR_C_CH2 -> BOOT0_CH2
- TP25 pad 1: SWDIO_CH2 -> +3V3
- TP26 pad 1: SWCLK_CH2 -> MOTOR_A_CH2
- TP27 pad 1: MOTOR_A_CH3 -> MOTOR_B_CH2
- TP28 pad 1: MOTOR_B_CH3 -> MOTOR_C_CH2
- TP29 pad 1: MOTOR_C_CH3 -> SWDIO_CH2
- TP30 pad 1: SWDIO_CH3 -> SWCLK_CH2
- TP31 pad 1: SWCLK_CH3 -> BOOT0_CH3
- TP32 pad 1: MOTOR_A_CH4 -> +3V3
- TP33 pad 1: MOTOR_B_CH4 -> MOTOR_A_CH3
- TP34 pad 1: MOTOR_C_CH4 -> MOTOR_B_CH3
- TP35 pad 1: SWDIO_CH4 -> MOTOR_C_CH3
- TP36 pad 1: SWCLK_CH4 -> SWDIO_CH3
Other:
- board text added: "+3V3"
- board text added: "+5V"
- board text added: "+9V"
- board text added: "A"
- board text added: "AI"
- board text added: "B"
- board text added: "BAT+"
- board text added: "BEC"
- board text added: "C"
- board text added: "CH1"
- board text added: "CH2"
- board text added: "CH3"
- board text added: "CH4"
- board text added: "CURR"
- board text added: "FC"
- board text added: "FC CONNECTOR"
- board text added: "GND"
- board text added: "M1"
- board text added: "M2"
- board text added: "M3"
- board text added: "M4"
- board text added: "NTC ICL"
- board text added: "PHASE3B-MOTOR-RELIEF-BEGIN"
- board text added: "PHASE3B-MOTOR-RELIEF-END"
- board text added: "PHASE3B-SILK-BEGIN"
- board text added: "PHASE3B-SILK-END"
- board text added: "PWR"
- board text added: "Pi5"
- board text added: "REV!"
- board text added: "Rev A"
- board text added: "SWCLK"
- board text added: "SWDIO"
- board text added: "THERMAL PADS UP TO HEATSINK"
- board text added: "TLM"
- board text added: "TP"
- board text added: "VBAT"
- board text added: "VTX1"
- board text added: "VTX2"
- board text added: "[MFR-MARK]"
- board text added: "^"
- board text added: "pcb.ai FPV4in1 v0"
